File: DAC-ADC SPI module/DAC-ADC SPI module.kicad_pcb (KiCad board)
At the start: 2 copper layers, 22.9 x 26.7 mm, 13 parts, among them J1 Conn_01x04_Male, J2 Conn_01x08_Male, J4 Conn_01x02_Male, U1 MCP1501, U2 MCP3204, U3 MCP4822

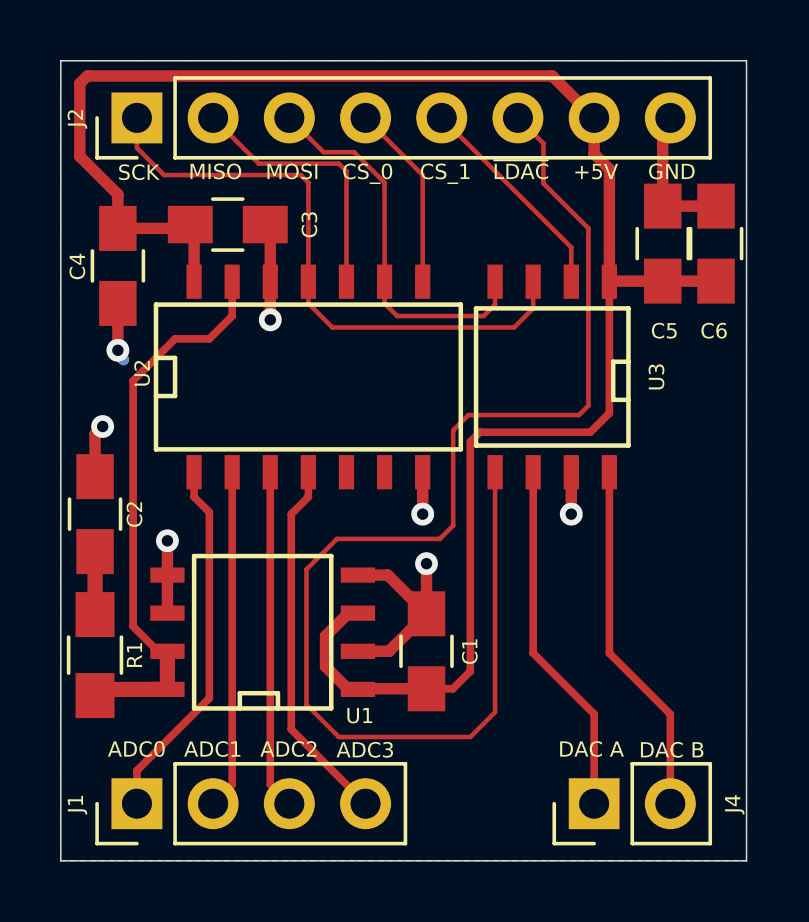
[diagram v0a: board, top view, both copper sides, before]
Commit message: Added top layer copper pours
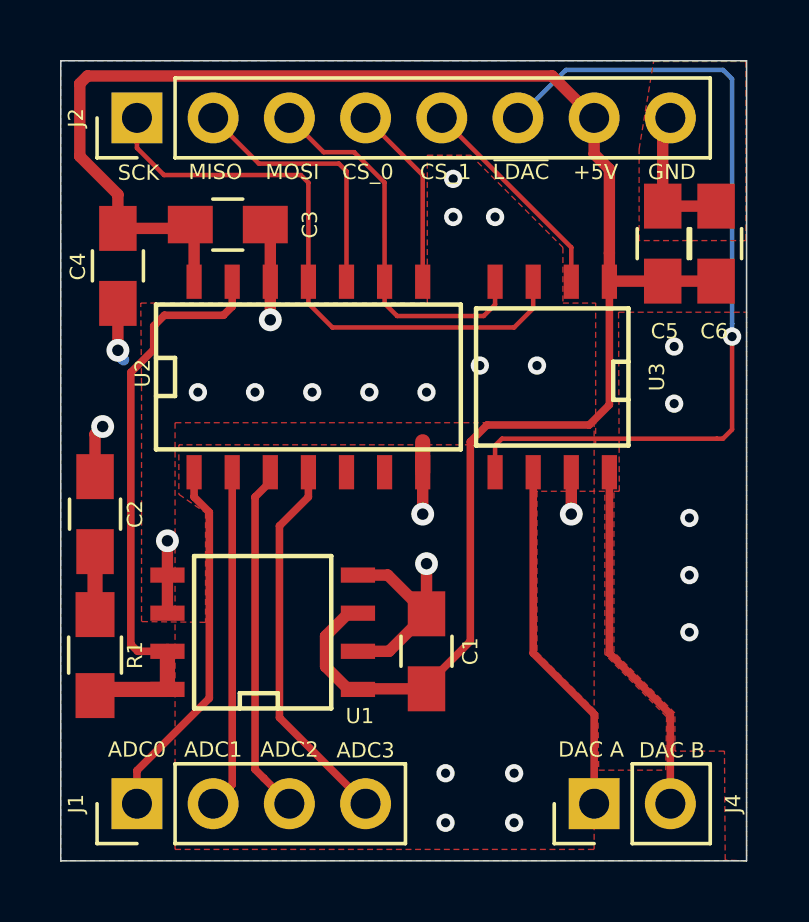
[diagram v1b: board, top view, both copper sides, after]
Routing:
- net /~LDAC: track 43.7 -> 28.6 mm, vias 0 -> 1
- net /Vref: track 18.8 -> 20.0 mm
- net GND: track 24.3 -> 25.3 mm, vias 7 -> 26
- net +5V: track 61.7 -> 61.0 mm
- added copper zone on F.Cu, net GND

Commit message: Silk screen edit
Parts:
- J1, J2, J4: moved to B.Cu
- turned J1 to 270 degrees
- turned J2 to 270 degrees
- turned J4 to 270 degrees
